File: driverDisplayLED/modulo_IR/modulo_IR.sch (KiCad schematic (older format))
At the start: 17 parts

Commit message: update
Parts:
- removed H? (x2): MountingHole, symbol Mechanical:MountingHole
- C2: renamed from C?; value C -> 104
- RV1: renamed from RV?; value R_POT -> 20K; PartNumber (none) -> 3362P-203LF-ND
- gave numbers to parts that had none: 13
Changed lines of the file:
@@
 $EndDescr
 $Comp
-L Device:C C?
+L Device:C C1
 U 1 1 5F9F8CCD
 P 2540 3500
-F 0 "C?" H 2655 3546 50  0000 L CNN
+F 0 "C1" H 2655 3546 50  0000 L CNN
 F 1 "104" H 2655 3455 50  0000 L CNN
 F 2 "" H 2578 3350 50  0001 C CNN
@@
 $EndComp
 $Comp
-L Device:LED D?
+L Device:LED D1
 U 1 1 5F9F90C6
 P 2970 3480
-F 0 "D?" V 3009 3362 50  0000 R CNN
+F 0 "D1" V 3009 3362 50  0000 R CNN
 F 1 "LED" V 2918 3362 50  0000 R CNN
 F 2 "" H 2970 3480 50  0001 C CNN
@@
 $EndComp
 $Comp
-L Comparator:LM393 U?
+L Comparator:LM393 U2
 U 1 1 5F9F97F0
 P 6320 3620
-F 0 "U?" H 6320 3987 50  0000 C CNN
+F 0 "U2" H 6320 3987 50  0000 C CNN
 F 1 "LM393" H 6320 3896 50  0000 C CNN
 F 2 "" H 6320 3620 50  0001 C CNN
@@
 $EndComp
 $Comp
-L Connector:Conn_01x03_Male J?
+L Connector:Conn_01x03_Male J1
 U 1 1 5F9FAFDC
 P 10160 4170
-F 0 "J?" H 10268 4451 50  0000 C CNN
+F 0 "J1" H 10268 4451 50  0000 C CNN
 F 1 "Conn_01x03_Male" H 10268 4360 50  0000 C CNN
 F 2 "" H 10160 4170 50  0001 C CNN
@@
 $EndComp
 $Comp
-L power:+5V #PWR?
+L power:+5V #PWR06
 U 1 1 5F9FB4CA
 P 5190 4190
-F 0 "#PWR?" H 5190 4040 50  0001 C CNN
+F 0 "#PWR06" H 5190 4040 50  0001 C CNN
 F 1 "+5V" H 5205 4363 50  0000 C CNN
 F 2 "" H 5190 4190 50  0001 C CNN
@@
 $EndComp
 $Comp
-L power:GND #PWR?
+L power:GND #PWR02
 U 1 1 5F9FBBF4
 P 2760 4310
-F 0 "#PWR?" H 2760 4060 50  0001 C CNN
+F 0 "#PWR02" H 2760 4060 50  0001 C CNN
 F 1 "GND" H 2765 4137 50  0000 C CNN
 F 2 "" H 2760 4310 50  0001 C CNN
@@
 $EndComp
 $Comp
-L Device:R R?
+L Device:R R4
 U 1 1 5F9FCABF
 P 5790 3230
-F 0 "R?" H 5860 3276 50  0000 L CNN
+F 0 "R4" H 5860 3276 50  0000 L CNN
 F 1 "10K" H 5860 3185 50  0000 L CNN
 F 2 "" V 5720 3230 50  0001 C CNN
@@
 $EndComp
 $Comp
-L Device:LED D?
+L Device:LED D2
 U 1 1 5F9FCF9A
 P 3500 3470
-F 0 "D?" V 3539 3352 50  0000 R CNN
+F 0 "D2" V 3539 3352 50  0000 R CNN
 F 1 "LED" V 3448 3352 50  0000 R CNN
 F 2 "" H 3500 3470 50  0001 C CNN
@@
 $EndComp
 $Comp
-L Device:C C?
+L Device:C C2
 U 1 1 5F9FD5B9
 P 6090 5110
-F 0 "C?" H 6205 5156 50  0000 L CNN
-F 1 "C" H 6205 5065 50  0000 L CNN
+F 0 "C2" H 6205 5156 50  0000 L CNN
+F 1 "104" H 6205 5065 50  0000 L CNN
 F 2 "" H 6128 4960 50  0001 C CNN
 F 3 "~" H 6090 5110 50  0001 C CNN
@@
 $EndComp
 $Comp
-L Device:R_POT RV?
+L Device:R_POT RV1
 U 1 1 5FA0095E
 P 4800 3720
-F 0 "RV?" H 4731 3766 50  0000 R CNN
-F 1 "R_POT" H 4731 3675 50  0000 R CNN
+F 0 "RV1" H 4731 3766 50  0000 R CNN
+F 1 "20K" H 4731 3675 50  0000 R CNN
 F 2 "" H 4800 3720 50  0001 C CNN
-F 3 "~" H 4800 3720 50  0001 C CNN
+F 3 "https://www.digikey.com/datasheets/bournsinc/bourns-inc-3362" H 4800 3720 50  0001 C CNN
+F 4 "3362P-203LF-ND" H 4800 3720 50  0001 C CNN "PartNumber"
 	1    4800 3720
 	1    0    0    -1
 $EndComp
 $Comp
-L power:+5V #PWR?
+L power:+5V #PWR01
 U 1 1 5FA0105A
 P 2730 3090
-F 0 "#PWR?" H 2730 2940 50  0001 C CNN
+F 0 "#PWR01" H 2730 2940 50  0001 C CNN
 F 1 "+5V" H 2745 3263 50  0000 C CNN
 F 2 "" H 2730 3090 50  0001 C CNN
@@
 $EndComp
 $Comp
-L Device:R R?
+L Device:R R1
 U 1 1 5FA074D2
 P 2970 4010
-F 0 "R?" H 3040 4056 50  0000 L CNN
+F 0 "R1" H 3040 4056 50  0000 L CNN
 F 1 "1K" H 3040 3965 50  0000 L CNN
 F 2 "" V 2900 4010 50  0001 C CNN
@@
 	2540 4310 2760 4310
 $Comp
-L Device:R R?
+L Device:R R3
 U 1 1 5FA0E964
 P 5190 4540
-F 0 "R?" H 5260 4586 50  0000 L CNN
+F 0 "R3" H 5260 4586 50  0000 L CNN
 F 1 "100" H 5260 4495 50  0000 L CNN
 F 2 "" V 5120 4540 50  0001 C CNN
@@
 Connection ~ 5790 5500
 $Comp
-L power:GND #PWR?
+L power:GND #PWR08
 U 1 1 5FA233CA
 P 5790 5570
-F 0 "#PWR?" H 5790 5320 50  0001 C CNN
+F 0 "#PWR08" H 5790 5320 50  0001 C CNN
 F 1 "GND" H 5795 5397 50  0000 C CNN
 F 2 "" H 5790 5570 50  0001 C CNN
@@
 	6020 3720 4950 3720
 $Comp
-L power:+5V #PWR?
+L power:+5V #PWR07
 U 1 1 5FA2C568
 P 5790 2930
-F 0 "#PWR?" H 5790 2780 50  0001 C CNN
+F 0 "#PWR07" H 5790 2780 50  0001 C CNN
 F 1 "+5V" H 5805 3103 50  0000 C CNN
 F 2 "" H 5790 2930 50  0001 C CNN
@@
 	5790 3080 5790 2930
 $Comp
-L power:+5V #PWR?
+L power:+5V #PWR04
 U 1 1 5FA324AF
 P 4800 2910
-F 0 "#PWR?" H 4800 2760 50  0001 C CNN
+F 0 "#PWR04" H 4800 2760 50  0001 C CNN
 F 1 "+5V" H 4815 3083 50  0000 C CNN
 F 2 "" H 4800 2910 50  0001 C CNN
@@
 	4800 2910 4800 3570
 $Comp
-L power:GND #PWR?
+L power:GND #PWR05
 U 1 1 5FA3993C
 P 4800 4010
-F 0 "#PWR?" H 4800 3760 50  0001 C CNN
+F 0 "#PWR05" H 4800 3760 50  0001 C CNN
 F 1 "GND" H 4805 3837 50  0000 C CNN
 F 2 "" H 4800 4010 50  0001 C CNN
@@
 	5190 4890 5190 4690
 $Comp
-L Isolator:SFH617A-1X001 U?
+L Isolator:SFH617A-1X001 U1
 U 1 1 5F9FA1B9
 P 5490 4990
-F 0 "U?" H 5490 5315 50  0000 C CNN
+F 0 "U1" H 5490 5315 50  0000 C CNN
 F 1 "SFH617A-1X001" H 5490 5224 50  0000 C CNN
 F 2 "Package_DIP:DIP-4_W7.62mm" H 5290 4790 50  0001 L CIN
@@
 Connection ~ 5790 3520
 $Comp
-L Device:R R?
+L Device:R R5
 U 1 1 5FA5B713
 P 6930 3230
-F 0 "R?" H 7000 3276 50  0000 L CNN
+F 0 "R5" H 7000 3276 50  0000 L CNN
 F 1 "10K" H 7000 3185 50  0000 L CNN
 F 2 "" V 6860 3230 50  0001 C CNN
@@
 $EndComp
 $Comp
-L power:+5V #PWR?
+L power:+5V #PWR09
 U 1 1 5FA5B719
 P 6930 2930
-F 0 "#PWR?" H 6930 2780 50  0001 C CNN
+F 0 "#PWR09" H 6930 2780 50  0001 C CNN
 F 1 "+5V" H 6945 3103 50  0000 C CNN
 F 2 "" H 6930 2930 50  0001 C CNN
@@
 Connection ~ 6930 3620
 $Comp
-L power:+5V #PWR?
+L power:+5V #PWR03
 U 1 1 5FA64015
 P 3500 3080
-F 0 "#PWR?" H 3500 2930 50  0001 C CNN
+F 0 "#PWR03" H 3500 2930 50  0001 C CNN
 F 1 "+5V" H 3515 3253 50  0000 C CNN
 F 2 "" H 3500 3080 50  0001 C CNN
@@
 $EndComp
 $Comp
-L power:+5V #PWR?
+L power:+5V #PWR010
 U 1 1 5FA66010
 P 10730 3930
-F 0 "#PWR?" H 10730 3780 50  0001 C CNN
+F 0 "#PWR010" H 10730 3780 50  0001 C CNN
 F 1 "+5V" H 10745 4103 50  0000 C CNN
 F 2 "" H 10730 3930 50  0001 C CNN
@@
 $EndComp
 $Comp
-L power:GND #PWR?
+L power:GND #PWR011
 U 1 1 5FA67442
 P 10740 4360
-F 0 "#PWR?" H 10740 4110 50  0001 C CNN
+F 0 "#PWR011" H 10740 4110 50  0001 C CNN
 F 1 "GND" H 10745 4187 50  0000 C CNN
 F 2 "" H 10740 4360 50  0001 C CNN
@@
 	10730 4070 10730 3930
 $Comp
-L Mechanical:MountingHole H?
+L Mechanical:MountingHole H1
 U 1 1 5FA6F62D
 P 10270 5180
-F 0 "H?" H 10370 5226 50  0000 L CNN
+F 0 "H1" H 10370 5226 50  0000 L CNN
 F 1 "MountingHole" H 10370 5135 50  0000 L CNN
 F 2 "" H 10270 5180 50  0001 C CNN
@@
 $EndComp
 $Comp
-L Mechanical:MountingHole H?
+L Mechanical:MountingHole H2
 U 1 1 5FA70E47
 P 10280 5490
-F 0 "H?" H 10380 5536 50  0000 L CNN
+F 0 "H2" H 10380 5536 50  0000 L CNN
 F 1 "MountingHole" H 10380 5445 50  0000 L CNN
 F 2 "" H 10280 5490 50  0001 C CNN
@@
 	1    0    0    -1
 $EndComp
-$Comp
-L Mechanical:MountingHole H?
-U 1 1 5FA72369
-P 10290 5820
-F 0 "H?" H 10390 5866 50  0000 L CNN
-F 1 "MountingHole" H 10390 5775 50  0000 L CNN
-F 2 "" H 10290 5820 50  0001 C CNN
-F 3 "~" H 10290 5820 50  0001 C CNN
-	1    10290 5820
-	1    0    0    -1
-$EndComp
-$Comp
-L Mechanical:MountingHole H?
-U 1 1 5FA7236F
-P 10300 6130
-F 0 "H?" H 10400 6176 50  0000 L CNN
-F 1 "MountingHole" H 10400 6085 50  0000 L CNN
-F 2 "" H 10300 6130 50  0001 C CNN
-F 3 "~" H 10300 6130 50  0001 C CNN
-	1    10300 6130
-	1    0    0    -1
-$EndComp
 Wire Wire Line
 	6930 3620 7640 3620
@@
 	3500 4110 3500 4300
 $Comp
-L Device:R R?
+L Device:R R2
 U 1 1 5F9FC3E7
 P 3500 3960
-F 0 "R?" H 3570 4006 50  0000 L CNN
+F 0 "R2" H 3570 4006 50  0000 L CNN
 F 1 "1K" H 3570 3915 50  0000 L CNN
 F 2 "" V 3430 3960 50  0001 C CNN

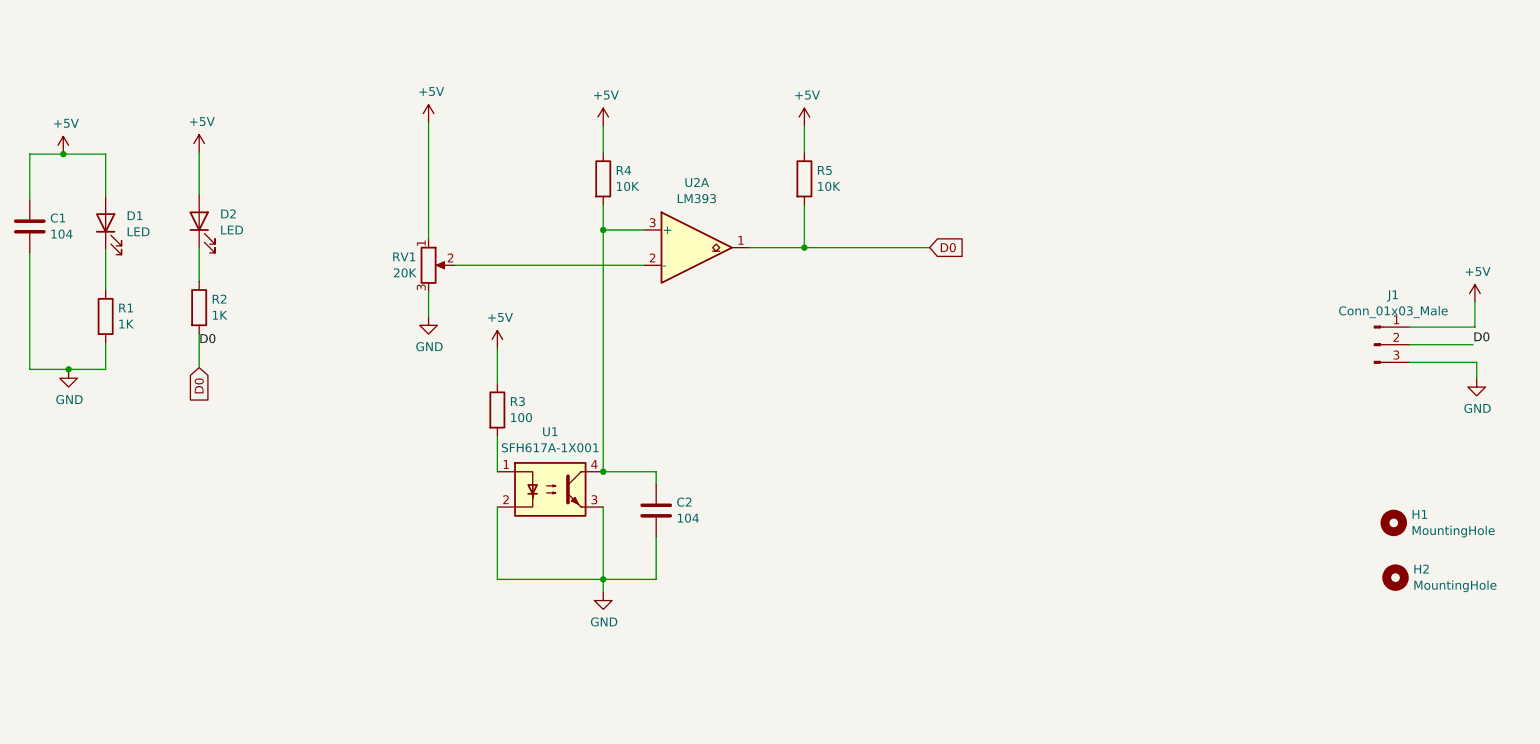
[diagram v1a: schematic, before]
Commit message: Correcciones basadas en la revisión del esquemático.
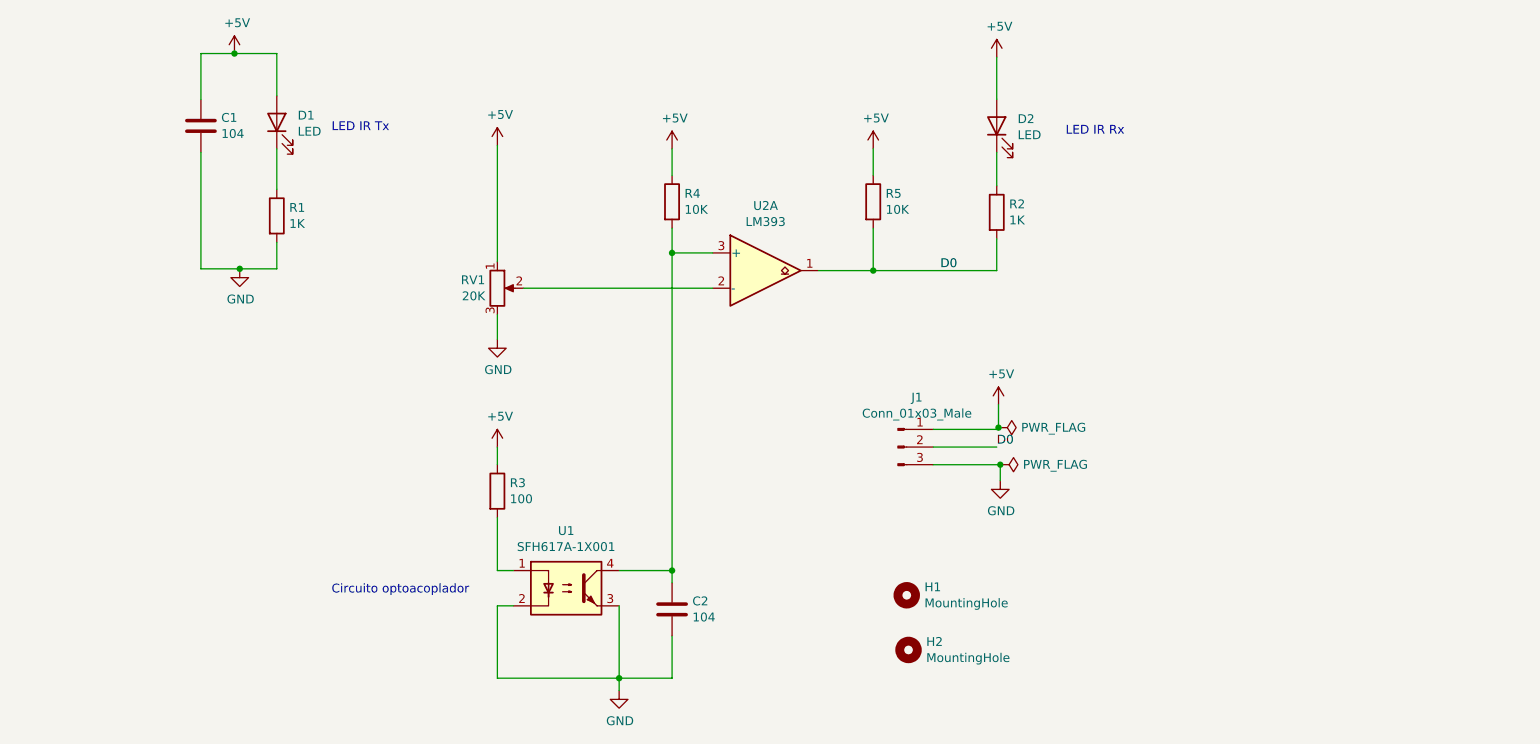
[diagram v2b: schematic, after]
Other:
- note added: "Circuito optoacoplador"
- note added: "LED IR Rx\n"
- note added: "LED IR Tx\n"
- moved on the sheet: C1, C2, D1, D2, H1, H2, J1, R1, R2, R3, R4, R5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

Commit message: Part numbers.
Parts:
- D1: Catalogue (none) -> Digikey 1080-1071-ND
- D2: Catalogue (none) -> Digikey 1516-1001-ND
- U1: Catalogue (none) -> Digikey SFH617A-3-ND
- U2: Catalogue (none) -> Digikey 2156-LM393N-ON-ND
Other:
- note added: "Fiduciales"
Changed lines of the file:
@@
 F 1 "LED" V 3888 2792 50  0000 R CNN
 F 2 "" H 3940 2910 50  0001 C CNN
-F 3 "~" H 3940 2910 50  0001 C CNN
+F 3 "www.everlight.com/file/ProductFile/201407061516067600.pdf" H 3940 2910 50  0001 C CNN
+F 4 "Digikey 1080-1071-ND" V 3940 2910 50  0001 C CNN "Catalogue"
 	1    3940 2910
 	0    -1   -1   0
@@
 F 1 "LM393" H 6710 4026 50  0000 C CNN
 F 2 "" H 6710 3750 50  0001 C CNN
-F 3 "http://www.ti.com/lit/ds/symlink/lm393.pdf" H 6710 3750 50  0001 C CNN
+F 3 "https://www.onsemi.com/pub/Collateral/LM293A-D.pdf" H 6710 3750 50  0001 C CNN
+F 4 "Digikey 2156-LM393N-ON-ND" H 6710 3750 50  0001 C CNN "Catalogue"
 	1    6710 3750
 	1    0    0    -1
@@
 F 1 "LED" V 7968 2812 50  0000 R CNN
 F 2 "" H 8020 2930 50  0001 C CNN
-F 3 "~" H 8020 2930 50  0001 C CNN
+F 3 "http://www.qt-brightek.com/datasheet/QBED8160.pdf" H 8020 2930 50  0001 C CNN
+F 4 "Digikey 1516-1001-ND" V 8020 2930 50  0001 C CNN "Catalogue"
 	1    8020 2930
 	0    -1   -1   0
@@
 F 2 "Package_DIP:DIP-4_W7.62mm" H 5380 5350 50  0001 L CIN
 F 3 "http://www.vishay.com/docs/83740/sfh617a.pdf" H 5580 5550 50  0001 L CNN
+F 4 "Digikey SFH617A-3-ND" H 5580 5550 50  0001 C CNN "Catalogue"
 	1    5580 5550
 	1    0    0    -1
@@
 $EndComp
 Connection ~ 8040 4850
+Text Notes 7500 6240 0    50   ~ 0
+Fiduciales
 $EndSCHEMATC

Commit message: asignacion de componentes
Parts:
- C1, C2: footprint (none) -> Capacitor_SMD:C_0504_1310Metric_Pad0.83x1.28mm_HandSolder
- D1, D2: footprint (none) -> LED_THT:LED_D1.8mm_W3.3mm_H2.4mm
- H1, H2: footprint (none) -> Fiducial:Fiducial_1mm_Mask2mm
- J1: footprint (none) -> Connector_PinHeader_2.54mm:PinHeader_1x03_P2.54mm_Vertical
- R1, R2, R3, R4, R5: footprint (none) -> Resistor_SMD:R_0805_2012Metric
- RV1: footprint (none) -> 3362P-1-103:TRIM_3362P-1-103
- U1: footprint Package_DIP:DIP-4_W7.62mm -> Package_SO:SO-4_7.6x3.6mm_P2.54mm
- U2: footprint (none) -> Package_SO:SOIC-8_3.9x4.9mm_P1.27mm
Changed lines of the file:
@@
 F 0 "C1" H 3625 2976 50  0000 L CNN
 F 1 "104" H 3625 2885 50  0000 L CNN
-F 2 "" H 3548 2780 50  0001 C CNN
+F 2 "Capacitor_SMD:C_0504_1310Metric_Pad0.83x1.28mm_HandSolder" H 3548 2780 50  0001 C CNN
 F 3 "~" H 3510 2930 50  0001 C CNN
 	1    3510 2930
@@
 F 0 "D1" V 3979 2792 50  0000 R CNN
 F 1 "LED" V 3888 2792 50  0000 R CNN
-F 2 "" H 3940 2910 50  0001 C CNN
+F 2 "LED_THT:LED_D1.8mm_W3.3mm_H2.4mm" H 3940 2910 50  0001 C CNN
 F 3 "www.everlight.com/file/ProductFile/201407061516067600.pdf" H 3940 2910 50  0001 C CNN
 F 4 "Digikey 1080-1071-ND" V 3940 2910 50  0001 C CNN "Catalogue"
@@
 F 0 "U2" H 6710 4117 50  0000 C CNN
 F 1 "LM393" H 6710 4026 50  0000 C CNN
-F 2 "" H 6710 3750 50  0001 C CNN
+F 2 "Package_SO:SOIC-8_3.9x4.9mm_P1.27mm" H 6710 3750 50  0001 C CNN
 F 3 "https://www.onsemi.com/pub/Collateral/LM293A-D.pdf" H 6710 3750 50  0001 C CNN
 F 4 "Digikey 2156-LM393N-ON-ND" H 6710 3750 50  0001 C CNN "Catalogue"
@@
 F 0 "J1" H 7568 5031 50  0000 C CNN
 F 1 "Conn_01x03_Male" H 7568 4940 50  0000 C CNN
-F 2 "" H 7460 4750 50  0001 C CNN
+F 2 "Connector_PinHeader_2.54mm:PinHeader_1x03_P2.54mm_Vertical" H 7460 4750 50  0001 C CNN
 F 3 "~" H 7460 4750 50  0001 C CNN
 	1    7460 4750
@@
 F 0 "R4" H 6250 3406 50  0000 L CNN
 F 1 "10K" H 6250 3315 50  0000 L CNN
-F 2 "" V 6110 3360 50  0001 C CNN
+F 2 "Resistor_SMD:R_0805_2012Metric" V 6110 3360 50  0001 C CNN
 F 3 "~" H 6180 3360 50  0001 C CNN
 	1    6180 3360
@@
 F 0 "D2" V 8059 2812 50  0000 R CNN
 F 1 "LED" V 7968 2812 50  0000 R CNN
-F 2 "" H 8020 2930 50  0001 C CNN
+F 2 "LED_THT:LED_D1.8mm_W3.3mm_H2.4mm" H 8020 2930 50  0001 C CNN
 F 3 "http://www.qt-brightek.com/datasheet/QBED8160.pdf" H 8020 2930 50  0001 C CNN
 F 4 "Digikey 1516-1001-ND" V 8020 2930 50  0001 C CNN "Catalogue"
@@
 F 0 "RV1" H 5121 3896 50  0000 R CNN
 F 1 "20K" H 5121 3805 50  0000 R CNN
-F 2 "" H 5190 3850 50  0001 C CNN
+F 2 "3362P-1-103:TRIM_3362P-1-103" H 5190 3850 50  0001 C CNN
 F 3 "https://www.digikey.com/datasheets/bournsinc/bourns-inc-3362" H 5190 3850 50  0001 C CNN
 F 4 "3362P-203LF-ND" H 5190 3850 50  0001 C CNN "PartNumber"
@@
 F 0 "R1" H 4010 3486 50  0000 L CNN
 F 1 "1K" H 4010 3395 50  0000 L CNN
-F 2 "" V 3870 3440 50  0001 C CNN
+F 2 "Resistor_SMD:R_0805_2012Metric" V 3870 3440 50  0001 C CNN
 F 3 "~" H 3940 3440 50  0001 C CNN
 	1    3940 3440
@@
 F 0 "R3" H 5260 5046 50  0000 L CNN
 F 1 "100" H 5260 4955 50  0000 L CNN
-F 2 "" V 5120 5000 50  0001 C CNN
+F 2 "Resistor_SMD:R_0805_2012Metric" V 5120 5000 50  0001 C CNN
 F 3 "~" H 5190 5000 50  0001 C CNN
 	1    5190 5000
@@
 F 0 "R5" H 7390 3406 50  0000 L CNN
 F 1 "10K" H 7390 3315 50  0000 L CNN
-F 2 "" V 7250 3360 50  0001 C CNN
+F 2 "Resistor_SMD:R_0805_2012Metric" V 7250 3360 50  0001 C CNN
 F 3 "~" H 7320 3360 50  0001 C CNN
 	1    7320 3360
@@
 F 0 "H1" H 7610 5636 50  0000 L CNN
 F 1 "MountingHole" H 7610 5545 50  0000 L CNN
-F 2 "" H 7510 5590 50  0001 C CNN
+F 2 "Fiducial:Fiducial_1mm_Mask2mm" H 7510 5590 50  0001 C CNN
 F 3 "~" H 7510 5590 50  0001 C CNN
 	1    7510 5590
@@
 F 0 "H2" H 7620 5946 50  0000 L CNN
 F 1 "MountingHole" H 7620 5855 50  0000 L CNN
-F 2 "" H 7520 5900 50  0001 C CNN
+F 2 "Fiducial:Fiducial_1mm_Mask2mm" H 7520 5900 50  0001 C CNN
 F 3 "~" H 7520 5900 50  0001 C CNN
 	1    7520 5900
@@
 F 0 "R2" H 8090 3466 50  0000 L CNN
 F 1 "1K" H 8090 3375 50  0000 L CNN
-F 2 "" V 7950 3420 50  0001 C CNN
+F 2 "Resistor_SMD:R_0805_2012Metric" V 7950 3420 50  0001 C CNN
 F 3 "~" H 8020 3420 50  0001 C CNN
 	1    8020 3420
@@
 F 0 "C2" H 6295 5716 50  0000 L CNN
 F 1 "104" H 6295 5625 50  0000 L CNN
-F 2 "" H 6218 5520 50  0001 C CNN
+F 2 "Capacitor_SMD:C_0504_1310Metric_Pad0.83x1.28mm_HandSolder" H 6218 5520 50  0001 C CNN
 F 3 "~" H 6180 5670 50  0001 C CNN
 	1    6180 5670
@@
 F 0 "U1" H 5580 5875 50  0000 C CNN
 F 1 "SFH617A-1X001" H 5580 5784 50  0000 C CNN
-F 2 "Package_DIP:DIP-4_W7.62mm" H 5380 5350 50  0001 L CIN
+F 2 "Package_SO:SO-4_7.6x3.6mm_P2.54mm" H 5380 5350 50  0001 L CIN
 F 3 "http://www.vishay.com/docs/83740/sfh617a.pdf" H 5580 5550 50  0001 L CNN
 F 4 "Digikey SFH617A-3-ND" H 5580 5550 50  0001 C CNN "Catalogue"

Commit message: placing components
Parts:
- U1: footprint Package_SO:SO-4_7.6x3.6mm_P2.54mm -> Package_SO:SO-4_4.4x2.3mm_P1.27mm
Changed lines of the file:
@@
 F 0 "U1" H 5580 5875 50  0000 C CNN
 F 1 "SFH617A-1X001" H 5580 5784 50  0000 C CNN
-F 2 "Package_SO:SO-4_7.6x3.6mm_P2.54mm" H 5380 5350 50  0001 L CIN
+F 2 "Package_SO:SO-4_4.4x2.3mm_P1.27mm" H 5380 5350 50  0001 L CIN
 F 3 "http://www.vishay.com/docs/83740/sfh617a.pdf" H 5580 5550 50  0001 L CNN
 F 4 "Digikey SFH617A-3-ND" H 5580 5550 50  0001 C CNN "Catalogue"
